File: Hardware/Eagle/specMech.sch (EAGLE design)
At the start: 86 parts, among them J1 PINHD-1X8-MOLEX-SHROUD, J2 JST-2-PIN-2B-PH-K-S(LF)(SN), J3 PINHD-1X8-MOLEX-SHROUD, J4 PINHD-1X8-MOLEX-SHROUD, J6 Molex 0022232081, J7 Lantronix XPORT, J8 Molex 0022232081, U1 MCP23008-E/SO, U10 ADS1115, U11 MCP23008-E/SO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

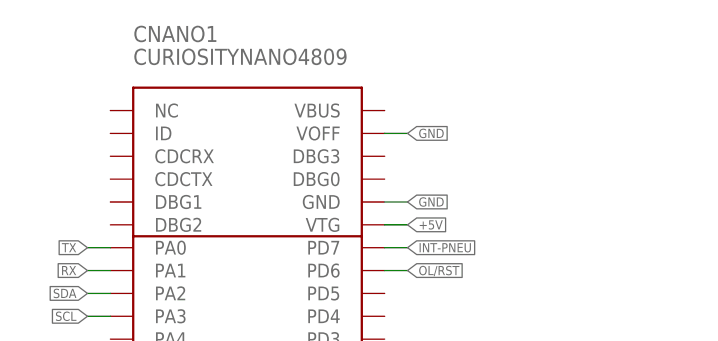
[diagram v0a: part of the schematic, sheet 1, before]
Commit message: Swapped castellated board in, starting rerouting
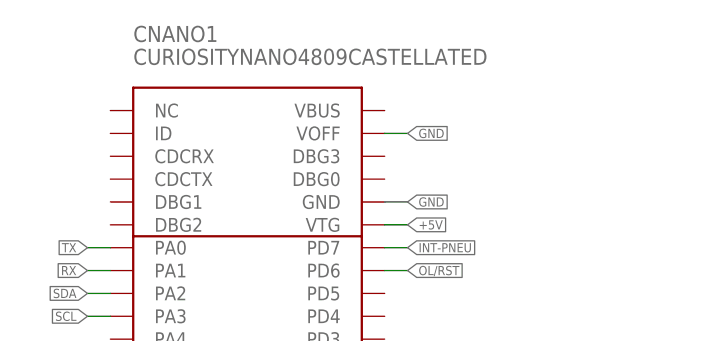
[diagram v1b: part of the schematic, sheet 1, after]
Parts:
- CNANO1: value CURIOSITYNANO4809 -> CURIOSITYNANO4809CASTELLATED; device AUmlib:CURIOSITYNANO4809 -> AUmlib:CURIOSITYNANO4809CASTELLATED
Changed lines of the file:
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@@
 <grid distance="0.1" unitdist="inch" unit="inch" style="lines" multiple="1" display="no" altdistance="0.01" altunitdist="inch" altunit="inch"/>
 <layers>
-<layer number="1" name="Top" color="4" fill="1" visible="no" active="no"/>
-<layer number="2" name="Route2" color="16" fill="1" visible="no" active="no"/>
-<layer number="3" name="Route3" color="17" fill="1" visible="no" active="no"/>
-<layer number="4" name="Route4" color="18" fill="1" visible="no" active="no"/>
-<layer number="5" name="Route5" color="19" fill="1" visible="no" active="no"/>
-<layer number="6" name="Route6" color="25" fill="1" visible="no" active="no"/>
-<layer number="7" name="Route7" color="26" fill="1" visible="no" active="no"/>
-<layer number="8" name="Route8" color="27" fill="1" visible="no" active="no"/>
-<layer number="9" name="Route9" color="28" fill="1" visible="no" active="no"/>
-<layer number="10" name="Route10" color="29" fill="1" visible="no" active="no"/>
-<layer number="11" name="Route11" color="30" fill="1" visible="no" active="no"/>
-<layer number="12" name="Route12" color="20" fill="1" visible="no" active="no"/>
-<layer number="13" name="Route13" color="21" fill="1" visible="no" active="no"/>
-<layer number="14" name="Route14" color="22" fill="1" visible="no" active="no"/>
-<layer number="15" name="Route15" color="23" fill="1" visible="no" active="no"/>
-<layer number="16" name="Bottom" color="1" fill="1" visible="no" active="no"/>
-<layer number="17" name="Pads" color="2" fill="1" visible="no" active="no"/>
-<layer number="18" name="Vias" color="2" fill="1" visible="no" active="no"/>
-<layer number="19" name="Unrouted" color="6" fill="1" visible="no" active="no"/>
-<layer number="20" name="Dimension" color="24" fill="1" visible="no" active="no"/>
-<layer number="21" name="tPlace" color="7" fill="1" visible="no" active="no"/>
-<layer number="22" name="bPlace" color="7" fill="1" visible="no" active="no"/>
-<layer number="23" name="tOrigins" color="15" fill="1" visible="no" active="no"/>
-<layer number="24" name="bOrigins" color="15" fill="1" visible="no" active="no"/>
-<layer number="25" name="tNames" color="7" fill="1" visible="no" active="no"/>
-<layer number="26" name="bNames" color="7" fill="1" visible="no" active="no"/>
-<layer number="27" name="tValues" color="7" fill="1" visible="no" active="no"/>
-<layer number="28" name="bValues" color="7" fill="1" visible="no" active="no"/>
+<layer number="1" name="Top" color="4" fill="1" visible="yes" active="no"/>
+<layer number="2" name="Route2" color="16" fill="1" visible="yes" active="no"/>
+<layer number="3" name="Route3" color="17" fill="1" visible="yes" active="no"/>
+<layer number="4" name="Route4" color="18" fill="1" visible="yes" active="no"/>
+<layer number="5" name="Route5" color="19" fill="1" visible="yes" active="no"/>
+<layer number="6" name="Route6" color="25" fill="1" visible="yes" active="no"/>
+<layer number="7" name="Route7" color="26" fill="1" visible="yes" active="no"/>
+<layer number="8" name="Route8" color="27" fill="1" visible="yes" active="no"/>
+<layer number="9" name="Route9" color="28" fill="1" visible="yes" active="no"/>
+<layer number="10" name="Route10" color="29" fill="1" visible="yes" active="no"/>
+<layer number="11" name="Route11" color="30" fill="1" visible="yes" active="no"/>
+<layer number="12" name="Route12" color="20" fill="1" visible="yes" active="no"/>
+<layer number="13" name="Route13" color="21" fill="1" visible="yes" active="no"/>
+<layer number="14" name="Route14" color="22" fill="1" visible="yes" active="no"/>
+<layer number="15" name="Route15" color="23" fill="1" visible="yes" active="no"/>
+<layer number="16" name="Bottom" color="1" fill="1" visible="yes" active="no"/>
+<layer number="17" name="Pads" color="2" fill="1" visible="yes" active="no"/>
+<layer number="18" name="Vias" color="2" fill="1" visible="yes" active="no"/>
+<layer number="19" name="Unrouted" color="6" fill="1" visible="yes" active="no"/>
+<layer number="20" name="Dimension" color="24" fill="1" visible="yes" active="no"/>
+<layer number="21" name="tPlace" color="7" fill="1" visible="yes" active="no"/>
+<layer number="22" name="bPlace" color="7" fill="1" visible="yes" active="no"/>
+<layer number="23" name="tOrigins" color="15" fill="1" visible="yes" active="no"/>
+<layer number="24" name="bOrigins" color="15" fill="1" visible="yes" active="no"/>
+<layer number="25" name="tNames" color="7" fill="1" visible="yes" active="no"/>
+<layer number="26" name="bNames" color="7" fill="1" visible="yes" active="no"/>
+<layer number="27" name="tValues" color="7" fill="1" visible="yes" active="no"/>
+<layer number="28" name="bValues" color="7" fill="1" visible="yes" active="no"/>
 <layer number="29" name="tStop" color="7" fill="3" visible="no" active="no"/>
 <layer number="30" name="bStop" color="7" fill="6" visible="no" active="no"/>
@@
 <layer number="35" name="tGlue" color="7" fill="4" visible="no" active="no"/>
 <layer number="36" name="bGlue" color="7" fill="5" visible="no" active="no"/>
-<layer number="37" name="tTest" color="7" fill="1" visible="no" active="no"/>
-<layer number="38" name="bTest" color="7" fill="1" visible="no" active="no"/>
+<layer number="37" name="tTest" color="7" fill="1" visible="yes" active="no"/>
+<layer number="38" name="bTest" color="7" fill="1" visible="yes" active="no"/>
 <layer number="39" name="tKeepout" color="4" fill="11" visible="no" active="no"/>
 <layer number="40" name="bKeepout" color="1" fill="11" visible="no" active="no"/>
@@
 <layer number="44" name="Drills" color="7" fill="1" visible="no" active="no"/>
 <layer number="45" name="Holes" color="7" fill="1" visible="no" active="no"/>
-<layer number="46" name="Milling" color="3" fill="1" visible="no" active="no"/>
-<layer number="47" name="Measures" color="7" fill="1" visible="no" active="no"/>
-<layer number="48" name="Document" color="7" fill="1" visible="no" active="no"/>
-<layer number="49" name="Reference" color="7" fill="1" visible="no" active="no"/>
-<layer number="50" name="dxf" color="7" fill="1" visible="no" active="no"/>
-<layer number="51" name="tDocu" color="7" fill="1" visible="no" active="no"/>
-<layer number="52" name="bDocu" color="7" fill="1" visible="no" active="no"/>
-<layer number="53" name="tGND_GNDA" color="7" fill="1" visible="no" active="no"/>
-<layer number="54" name="bGND_GNDA" color="7" fill="1" visible="no" active="no"/>
-<layer number="56" name="wert" color="7" fill="1" visible="no" active="no"/>
-<layer number="57" name="tCAD" color="7" fill="1" visible="no" active="no"/>
-<layer number="59" name="tCarbon" color="7" fill="1" visible="no" active="no"/>
-<layer number="60" name="bCarbon" color="7" fill="1" visible="no" active="no"/>
+<layer number="46" name="Milling" color="3" fill="1" visible="yes" active="no"/>
+<layer number="47" name="Measures" color="7" fill="1" visible="yes" active="no"/>
+<layer number="48" name="Document" color="7" fill="1" visible="yes" active="no"/>
+<layer number="49" name="Reference" color="7" fill="1" visible="yes" active="no"/>
+<layer number="50" name="dxf" color="7" fill="1" visible="yes" active="no"/>
+<layer number="51" name="tDocu" color="7" fill="1" visible="yes" active="no"/>
+<layer number="52" name="bDocu" color="7" fill="1" visible="yes" active="no"/>
+<layer number="53" name="tGND_GNDA" color="7" fill="1" visible="yes" active="no"/>
+<layer number="54" name="bGND_GNDA" color="7" fill="1" visible="yes" active="no"/>
+<layer number="56" name="wert" color="7" fill="1" visible="yes" active="no"/>
+<layer number="57" name="tCAD" color="7" fill="1" visible="yes" active="no"/>
+<layer number="59" name="tCarbon" color="7" fill="1" visible="yes" active="no"/>
+<layer number="60" name="bCarbon" color="7" fill="1" visible="yes" active="no"/>
 <layer number="88" name="SimResults" color="9" fill="1" visible="yes" active="yes"/>
 <layer number="89" name="SimProbes" color="9" fill="1" visible="yes" active="yes"/>
@@
 <part name="C1" library="AUmlib" library_urn="urn:adsk.eagle:library:9166017" deviceset="C-US" device="C0805" package3d_urn="urn:adsk.eagle:package:4021265/3" value="0.01uF"/>
 <part name="J1" library="AUmlib" library_urn="urn:adsk.eagle:library:9166017" deviceset="PINHD-1X8-MOLEX-SHROUD" device="" package3d_urn="urn:adsk.eagle:package:18132194/6"/>
-<part name="CNANO1" library="AUmlib" library_urn="urn:adsk.eagle:library:9166017" deviceset="CURIOSITYNANO4809" device="" package3d_urn="urn:adsk.eagle:package:15461704/5"/>
+<part name="CNANO1" library="AUmlib" library_urn="urn:adsk.eagle:library:9166017" deviceset="CURIOSITYNANO4809" device="CASTELLATED" package3d_urn="urn:adsk.eagle:package:15461731/6" value="CURIOSITYNANO4809CASTELLATED"/>
 <part name="FRAME1" library="frames" library_urn="urn:adsk.eagle:library:229" deviceset="FRAME_A_L" device="" value="Frame_A_L"/>
 <part name="FRAME3" library="frames" library_urn="urn:adsk.eagle:library:229" deviceset="FRAME_A_L" device="" value="Frame_A_L"/>

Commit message: More routing
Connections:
- new net N$27: J1.2
- net A0B: now also J4.1; no longer J4.2
- net A1B: now also J4.3; no longer J4.4
- net A2B: now also J4.5; no longer J4.6
- net A3B: now also J4.7; no longer J4.8
- net GND: now also J4.2, J4.4, J4.6, J4.8; no longer J4.1, J4.3, J4.5, J4.7
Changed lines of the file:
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@@
 <setting verticaltext="up"/>
 </settings>
-<grid distance="0.1" unitdist="inch" unit="inch" style="lines" multiple="1" display="no" altdistance="0.01" altunitdist="inch" altunit="inch"/>
+<grid distance="0.1" unitdist="inch" unit="inch" style="lines" multiple="1" display="yes" altdistance="0.01" altunitdist="inch" altunit="inch"/>
 <layers>
 <layer number="1" name="Top" color="4" fill="1" visible="yes" active="no"/>
@@
 <part name="TP6" library="AUmlib" library_urn="urn:adsk.eagle:library:9166017" deviceset="TP5000-TESTPOINT-ORG" device="" package3d_urn="urn:adsk.eagle:package:24643890/2"/>
 <part name="TP5" library="AUmlib" library_urn="urn:adsk.eagle:library:9166017" deviceset="TP5000-TESTPOINT-BLK" device="" package3d_urn="urn:adsk.eagle:package:24642442/4"/>
+<part name="U$1" library="AUmlib" library_urn="urn:adsk.eagle:library:9166017" deviceset="NC" device=""/>
 </parts>
 <sheets>
@@
 <attribute name="VALUE" x="93.98" y="93.98" size="1.778" layer="96"/>
 </instance>
+<instance part="U$1" gate="G$1" x="241.3" y="165.1" smashed="yes"/>
 </instances>
 <busses>
@@
 </segment>
 <segment>
-<pinref part="J4" gate="G$1" pin="7"/>
-<wire x1="236.22" y1="109.22" x2="243.84" y2="109.22" width="0.1524" layer="91"/>
-<wire x1="243.84" y1="109.22" x2="243.84" y2="104.14" width="0.1524" layer="91"/>
-<pinref part="J4" gate="G$1" pin="5"/>
-<wire x1="243.84" y1="104.14" x2="243.84" y2="99.06" width="0.1524" layer="91"/>
-<wire x1="243.84" y1="99.06" x2="243.84" y2="93.98" width="0.1524" layer="91"/>
-<wire x1="243.84" y1="93.98" x2="243.84" y2="88.9" width="0.1524" layer="91"/>
-<wire x1="236.22" y1="104.14" x2="243.84" y2="104.14" width="0.1524" layer="91"/>
-<junction x="243.84" y="104.14"/>
-<pinref part="J4" gate="G$1" pin="3"/>
-<wire x1="236.22" y1="99.06" x2="243.84" y2="99.06" width="0.1524" layer="91"/>
-<junction x="243.84" y="99.06"/>
-<pinref part="J4" gate="G$1" pin="1"/>
-<wire x1="236.22" y1="93.98" x2="243.84" y2="93.98" width="0.1524" layer="91"/>
-<junction x="243.84" y="93.98"/>
-<pinref part="GND35" gate="1" pin="GND"/>
-</segment>
-<segment>
 <pinref part="U10" gate="A" pin="GND"/>
 <wire x1="147.32" y1="96.52" x2="149.86" y2="96.52" width="0.1524" layer="91"/>
@@
 <wire x1="96.52" y1="101.6" x2="96.52" y2="99.06" width="0.1524" layer="91"/>
 <pinref part="GND45" gate="1" pin="GND"/>
+</segment>
+<segment>
+<pinref part="J4" gate="G$1" pin="8"/>
+<wire x1="236.22" y1="111.76" x2="243.84" y2="111.76" width="0.1524" layer="91"/>
+<pinref part="GND35" gate="1" pin="GND"/>
+<wire x1="243.84" y1="111.76" x2="243.84" y2="106.68" width="0.1524" layer="91"/>
+<pinref part="J4" gate="G$1" pin="6"/>
+<wire x1="243.84" y1="106.68" x2="243.84" y2="101.6" width="0.1524" layer="91"/>
+<wire x1="243.84" y1="101.6" x2="243.84" y2="96.52" width="0.1524" layer="91"/>
+<wire x1="243.84" y1="96.52" x2="243.84" y2="88.9" width="0.1524" layer="91"/>
+<wire x1="236.22" y1="106.68" x2="243.84" y2="106.68" width="0.1524" layer="91"/>
+<junction x="243.84" y="106.68"/>
+<pinref part="J4" gate="G$1" pin="4"/>
+<wire x1="236.22" y1="101.6" x2="243.84" y2="101.6" width="0.1524" layer="91"/>
+<junction x="243.84" y="101.6"/>
+<pinref part="J4" gate="G$1" pin="2"/>
+<wire x1="236.22" y1="96.52" x2="243.84" y2="96.52" width="0.1524" layer="91"/>
+<junction x="243.84" y="96.52"/>
 </segment>
 </net>
@@
 </segment>
 <segment>
-<pinref part="J4" gate="G$1" pin="2"/>
-<wire x1="236.22" y1="96.52" x2="246.38" y2="96.52" width="0.1524" layer="91"/>
-<label x="246.38" y="96.52" size="1.778" layer="95" xref="yes"/>
+<pinref part="J4" gate="G$1" pin="1"/>
+<wire x1="236.22" y1="93.98" x2="246.38" y2="93.98" width="0.1524" layer="91"/>
+<label x="246.38" y="93.98" size="1.778" layer="95" xref="yes"/>
 </segment>
 </net>
@@
 </segment>
 <segment>
-<pinref part="J4" gate="G$1" pin="4"/>
-<wire x1="236.22" y1="101.6" x2="246.38" y2="101.6" width="0.1524" layer="91"/>
-<label x="246.38" y="101.6" size="1.778" layer="95" xref="yes"/>
+<pinref part="J4" gate="G$1" pin="3"/>
+<wire x1="236.22" y1="99.06" x2="246.38" y2="99.06" width="0.1524" layer="91"/>
+<label x="246.38" y="99.06" size="1.778" layer="95" xref="yes"/>
 </segment>
 </net>
@@
 </segment>
 <segment>
-<pinref part="J4" gate="G$1" pin="6"/>
-<wire x1="236.22" y1="106.68" x2="246.38" y2="106.68" width="0.1524" layer="91"/>
-<label x="246.38" y="106.68" size="1.778" layer="95" xref="yes"/>
+<pinref part="J4" gate="G$1" pin="5"/>
+<wire x1="236.22" y1="104.14" x2="246.38" y2="104.14" width="0.1524" layer="91"/>
+<label x="246.38" y="104.14" size="1.778" layer="95" xref="yes"/>
 </segment>
 </net>
@@
 </segment>
 <segment>
-<pinref part="J4" gate="G$1" pin="8"/>
-<wire x1="236.22" y1="111.76" x2="246.38" y2="111.76" width="0.1524" layer="91"/>
-<label x="246.38" y="111.76" size="1.778" layer="95" xref="yes"/>
-</segment>
-</net>
+<pinref part="J4" gate="G$1" pin="7"/>
+<wire x1="236.22" y1="109.22" x2="246.38" y2="109.22" width="0.1524" layer="91"/>
+<label x="246.38" y="109.22" size="1.778" layer="95" xref="yes"/>
+</segment>
+</net>
+<net name="N$27" class="0">
+<segment>
+<pinref part="J1" gate="G$1" pin="2"/>
+<wire x1="236.22" y1="165.1" x2="241.3" y2="165.1" width="0.1524" layer="91"/>
+</segment>
+</net>

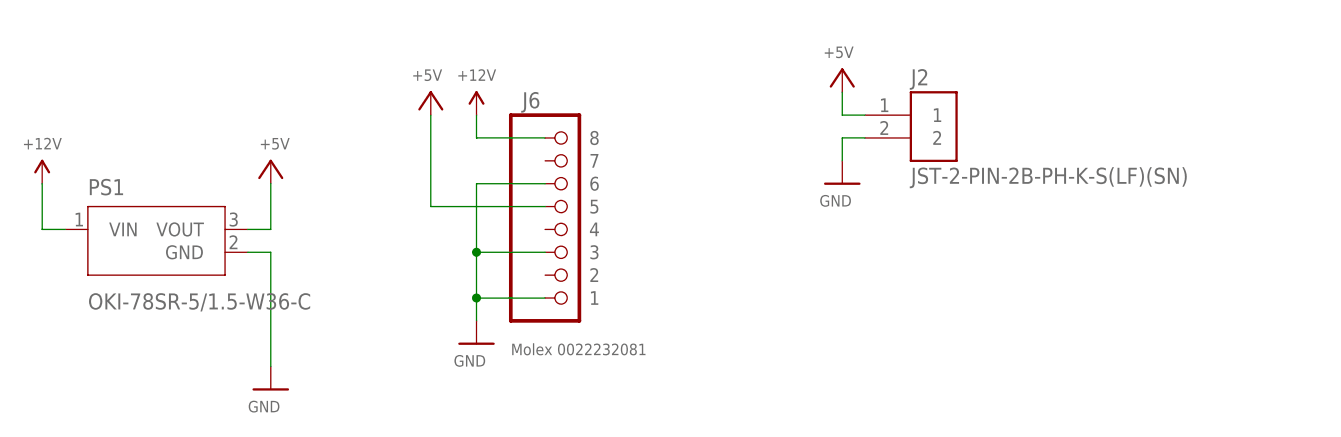
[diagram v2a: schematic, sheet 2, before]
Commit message: Molex 1x2 header replaces JST header
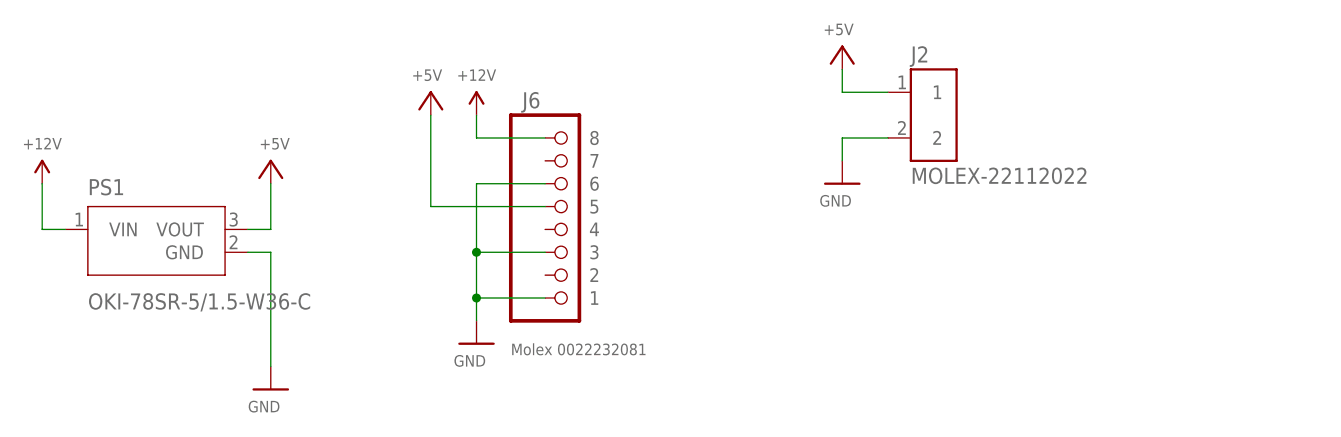
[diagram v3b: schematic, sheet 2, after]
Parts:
- J2: value JST-2-PIN-2B-PH-K-S(LF)(SN) -> MOLEX-22112022; device AUmlib:JST-2-PIN-2B-PH-K-S(LF)(SN) -> AUmlib:PINHD-1X2-MOLEX-22112022
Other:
- moved on the sheet: J2
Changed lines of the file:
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@@
 <part name="GND45" library="AUmlib" library_urn="urn:adsk.eagle:library:9166017" deviceset="GND" device=""/>
 <part name="J7" library="AUmlib" library_urn="urn:adsk.eagle:library:9166017" deviceset="XPORT" device="XPORT-2" package3d_urn="urn:adsk.eagle:package:18328251/5" value="Lantronix XPORT"/>
-<part name="J2" library="AUmlib" library_urn="urn:adsk.eagle:library:9166017" deviceset="JST-2-PIN-2B-PH-K-S(LF)(SN)" device="" package3d_urn="urn:adsk.eagle:package:24616272/2"/>
+<part name="J2" library="AUmlib" library_urn="urn:adsk.eagle:library:9166017" deviceset="PINHD-1X2-MOLEX-22112022" device="" package3d_urn="urn:adsk.eagle:package:24727026/5" value="MOLEX-22112022"/>
 <part name="GND4" library="AUmlib" library_urn="urn:adsk.eagle:library:9166017" deviceset="GND" device=""/>
 <part name="P+27" library="AUmlib" library_urn="urn:adsk.eagle:library:9166017" deviceset="+5V" device=""/>
@@
 </instance>
 <instance part="J2" gate="G$1" x="177.8" y="137.16" smashed="yes">
-<attribute name="NAME" x="175.255640625" y="140.46766875" size="1.78105" layer="95"/>
+<attribute name="NAME" x="175.255640625" y="143.00766875" size="1.78105" layer="95"/>
 <attribute name="VALUE" x="175.255409375" y="129.526240625" size="1.781209375" layer="96"/>
 </instance>
@@
 <attribute name="VALUE" x="165.1" y="127" size="1.27" layer="96"/>
 </instance>
-<instance part="P+27" gate="1" x="167.64" y="142.24" smashed="yes">
-<attribute name="VALUE" x="168.91" y="144.78" size="1.27" layer="96" rot="R180"/>
+<instance part="P+27" gate="1" x="167.64" y="144.78" smashed="yes">
+<attribute name="VALUE" x="168.91" y="147.32" size="1.27" layer="96" rot="R180"/>
 </instance>
 </instances>
@@
 <wire x1="167.64" y1="132.08" x2="167.64" y2="134.62" width="0.1524" layer="91"/>
 <pinref part="J2" gate="G$1" pin="2"/>
-<wire x1="167.64" y1="134.62" x2="170.18" y2="134.62" width="0.1524" layer="91"/>
+<wire x1="167.64" y1="134.62" x2="172.72" y2="134.62" width="0.1524" layer="91"/>
 </segment>
 </net>
@@
 <segment>
 <pinref part="J2" gate="G$1" pin="1"/>
-<wire x1="170.18" y1="137.16" x2="167.64" y2="137.16" width="0.1524" layer="91"/>
+<wire x1="172.72" y1="139.7" x2="167.64" y2="139.7" width="0.1524" layer="91"/>
 <pinref part="P+27" gate="1" pin="+5V"/>
-<wire x1="167.64" y1="137.16" x2="167.64" y2="139.7" width="0.1524" layer="91"/>
-</segment>
-</net>
+<wire x1="167.64" y1="139.7" x2="167.64" y2="142.24" width="0.1524" layer="91"/>
+</segment>
+</net>
